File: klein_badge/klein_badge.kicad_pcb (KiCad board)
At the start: 2 copper layers, 24 parts, among them J1 Conn_01x05, J2 Conn_01x05, U1 74AUC1G07

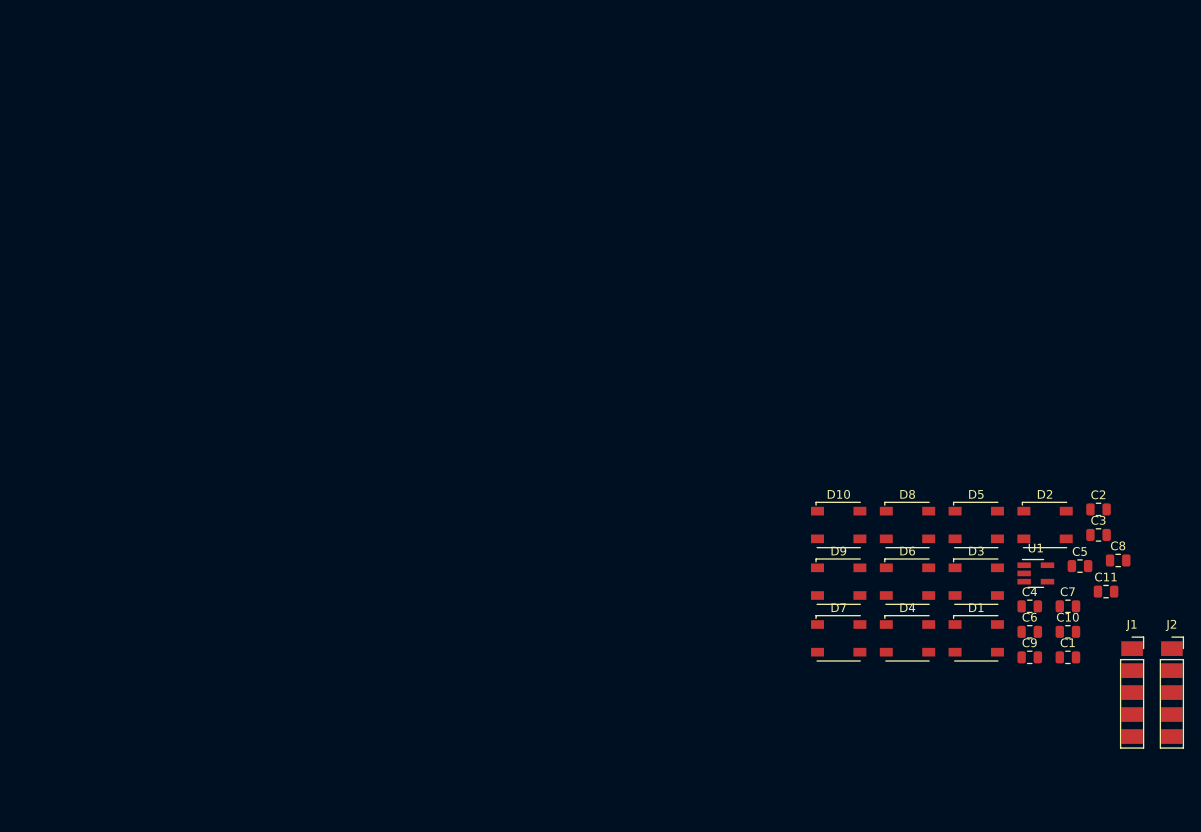
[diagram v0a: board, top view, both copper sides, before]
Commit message: Added images to get silkscreen, did rough layout.
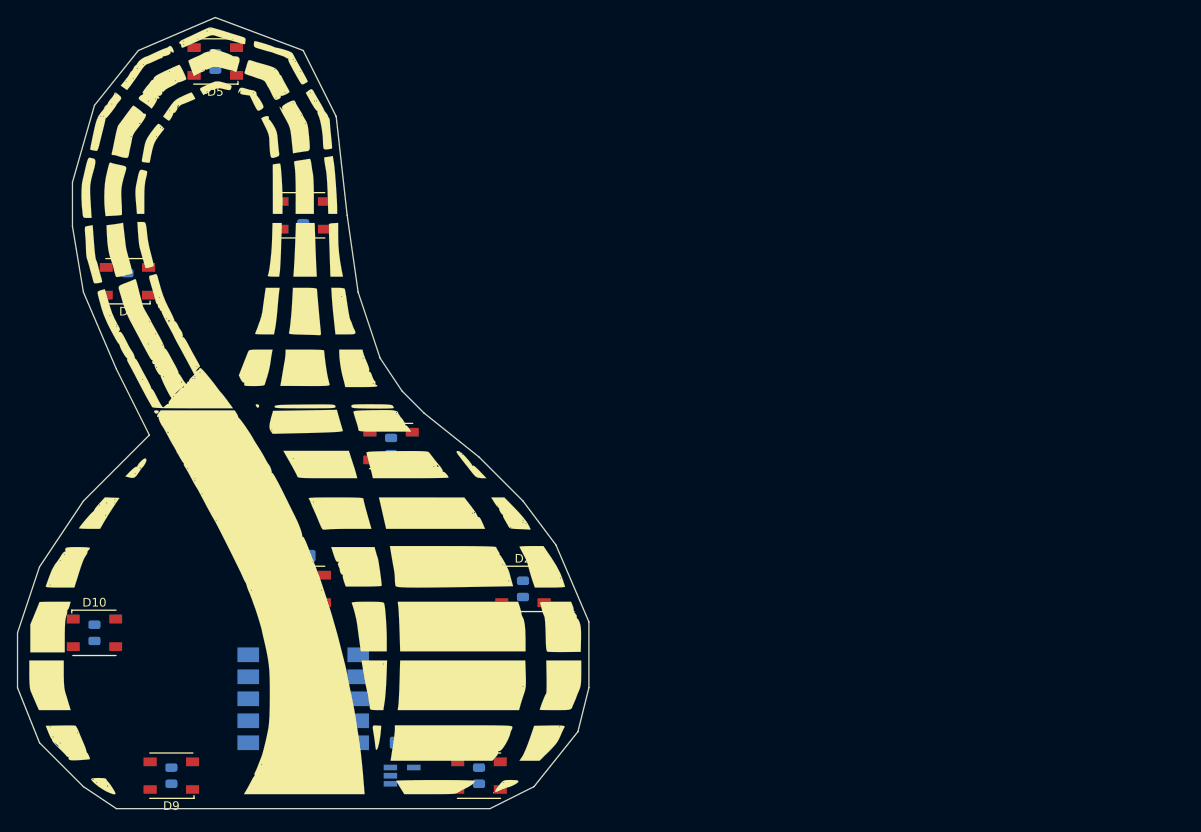
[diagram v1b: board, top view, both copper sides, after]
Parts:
- added G***: LOGO, headers:klein_image_negative_small, F.Cu at (62.2, 78.7)
- C1, C10, C11, C2, C3, C4, C5, C6, C7, C8, C9, J1, J2, U1: moved to B.Cu
- moved C11 119.8 mm to (48.3, 40.6), turned to 90 degrees
- moved C5 114.9 mm to (38.1, 66.0), turned to 90 degrees
- moved C2 111.5 mm to (43.2, 123.2), turned to 90 degrees
- moved C9 108.1 mm to (34.3, 106.7), turned to 270 degrees
- moved C8 106.6 mm to (47.0, 83.8), turned to 90 degrees
- moved D5 103.0 mm to (48.3, 40.6), turned to 180 degrees
- moved J1 102.7 mm to (52.1, 119.4)
- moved C7 99.3 mm to (58.4, 58.4), turned to 270 degrees
- moved D6 96.6 mm to (38.1, 66.0), turned to 180 degrees
- moved J2 94.7 mm to (64.8, 119.4)
- moved C3 92.0 mm to (58.4, 97.8), turned to 180 degrees
- moved D10 86.9 mm to (34.3, 106.7)
- moved D4 85.3 mm to (58.4, 58.4)
- moved C10 81.1 mm to (68.6, 85.1), turned to 270 degrees
- moved D9 80.3 mm to (43.2, 123.2), turned to 180 degrees
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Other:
- board outline added: 66 x 91.4 mm

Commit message: Finished routing.
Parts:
- moved C4 4.10 mm to (73.7, 120.9), turned to 270 degrees
- moved U1 2.30 mm to (70.1, 120.9)
- turned C1 to 0 degrees
- turned C10 to 0 degrees
- turned C5 to 180 degrees
- turned C7 to 0 degrees
- turned C8 to 180 degrees
- turned C9 to 0 degrees
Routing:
- net GND: track 0.00 -> 332.1 mm, vias 0 -> 10
- net +5V: track 0.00 -> 294.6 mm, vias 0 -> 10
- net Net-(J1-Pad3): track 0.00 -> 32.5 mm
- net Net-(D3-Pad4): track 0.00 -> 29.7 mm
- net Net-(D2-Pad4): track 0.00 -> 26.5 mm
- net Net-(D5-Pad4): track 0.00 -> 25.3 mm
- net Net-(D8-Pad4): track 0.00 -> 22.8 mm
- net Net-(D4-Pad4): track 0.00 -> 22.8 mm
- net Net-(D7-Pad4): track 0.00 -> 22.8 mm
- net Net-(D10-Pad2): track 0.00 -> 20.8 mm
- net Net-(D6-Pad4): track 0.00 -> 20.4 mm
- net Net-(D1-Pad4): track 0.00 -> 18.5 mm
- net Net-(D1-Pad2): track 0.00 -> 9.66 mm, vias 0 -> 1
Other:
- board text added: "Klein's Playground"
- board text added: "Klein's Playground Collective Burning Man 2019"
